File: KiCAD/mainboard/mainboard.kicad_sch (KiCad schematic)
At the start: 0 parts

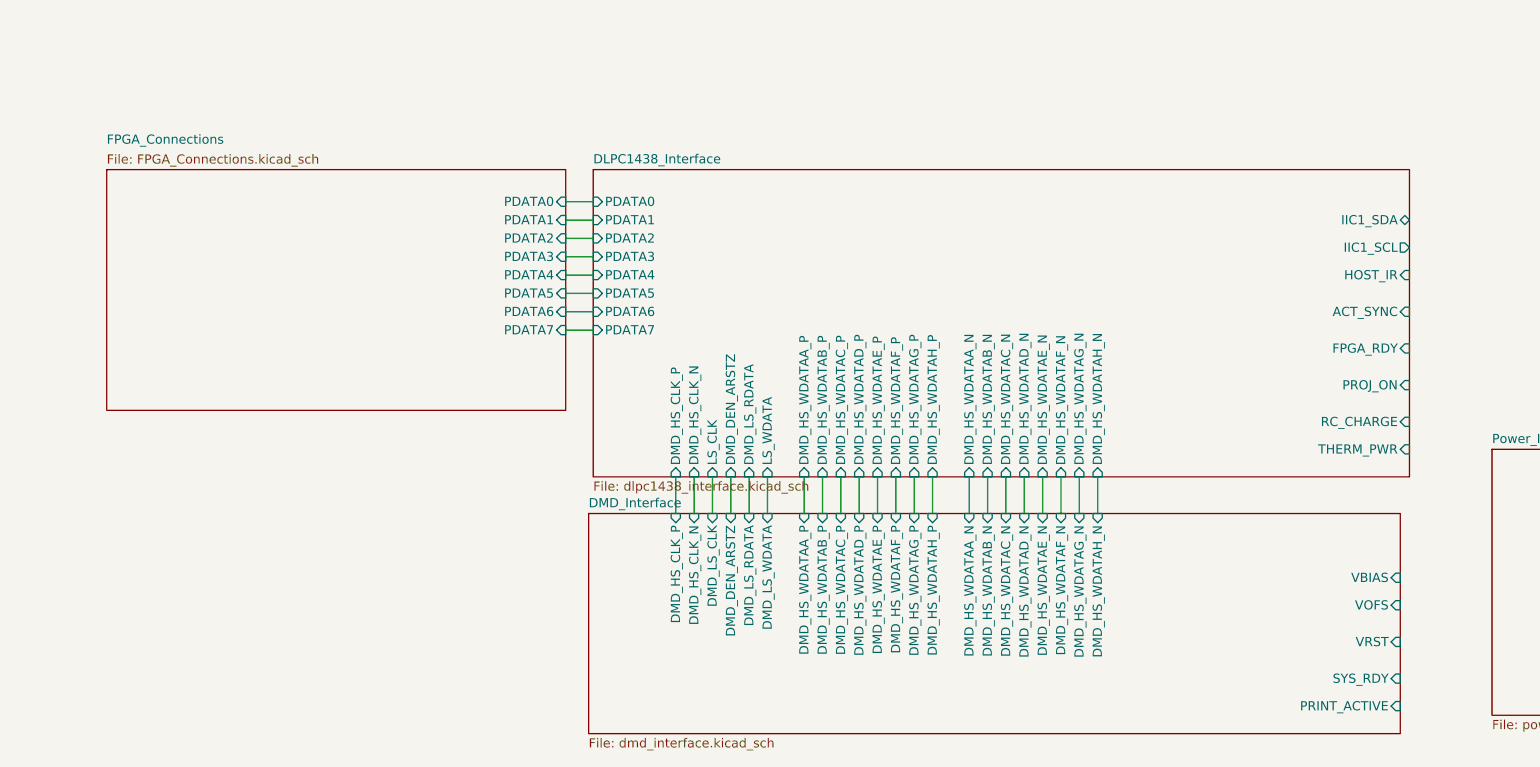
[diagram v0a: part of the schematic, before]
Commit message: fixed funny bus connectinos
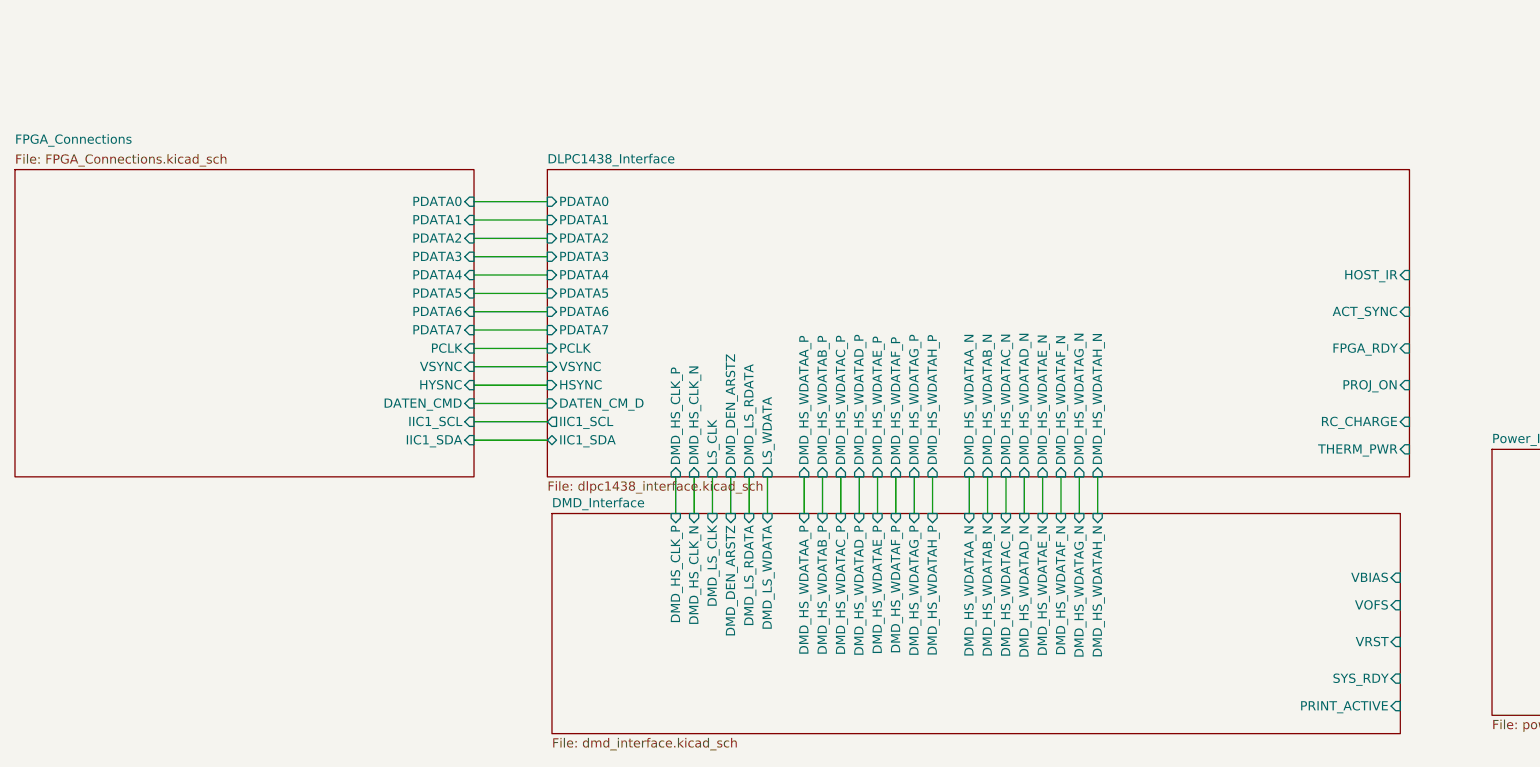
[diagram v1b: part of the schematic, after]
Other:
- sheet DLPC1438_Interface ports: added DATEN_CM_D, HSYNC, PCLK, VSYNC; removed none
- sheet FPGA_Connections ports: added DATEN_CMD, HYSNC, IIC1_SCL, IIC1_SDA, PCLK, VSYNC; removed none

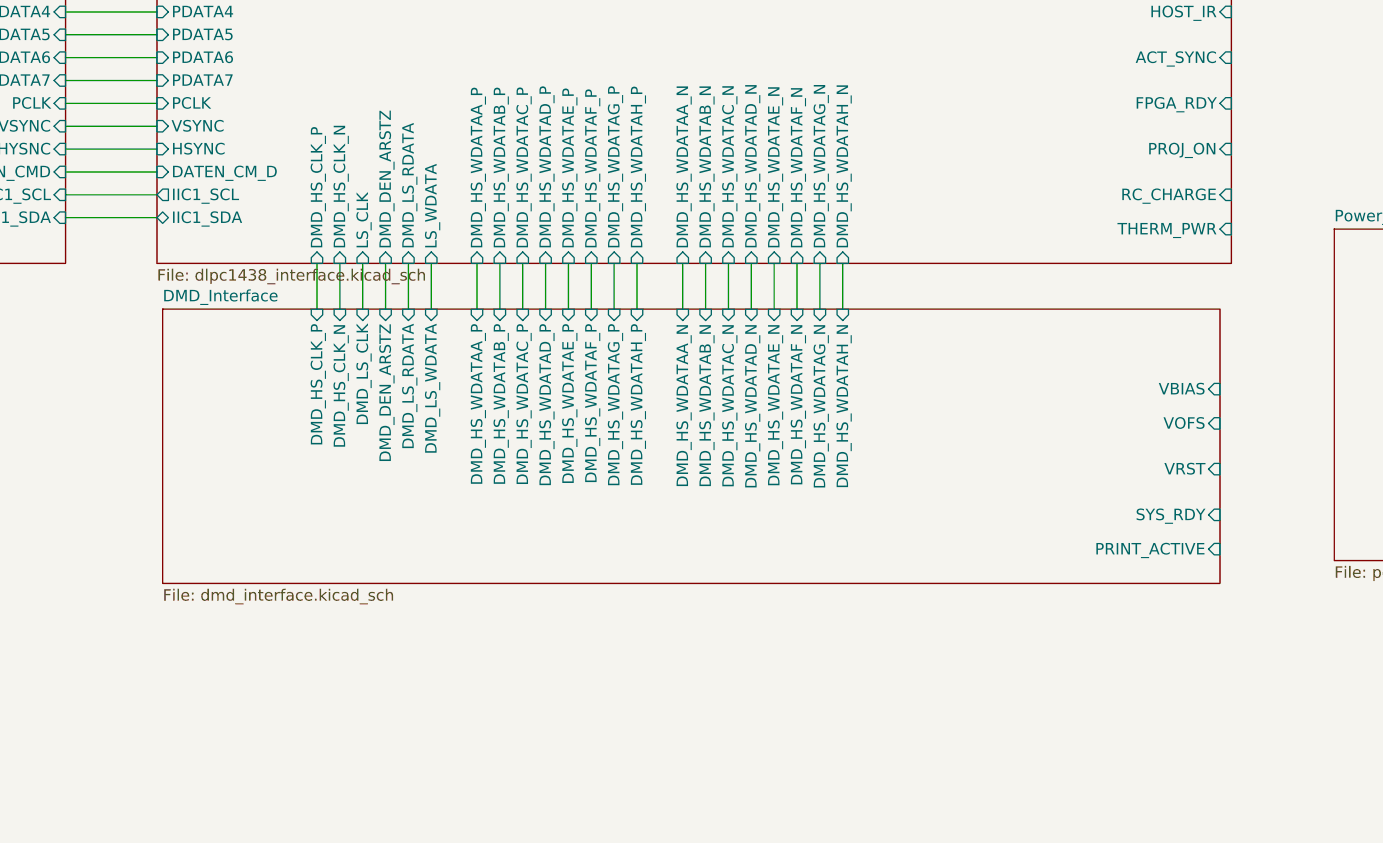
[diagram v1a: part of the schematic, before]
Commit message: gpios are now hierarchicals
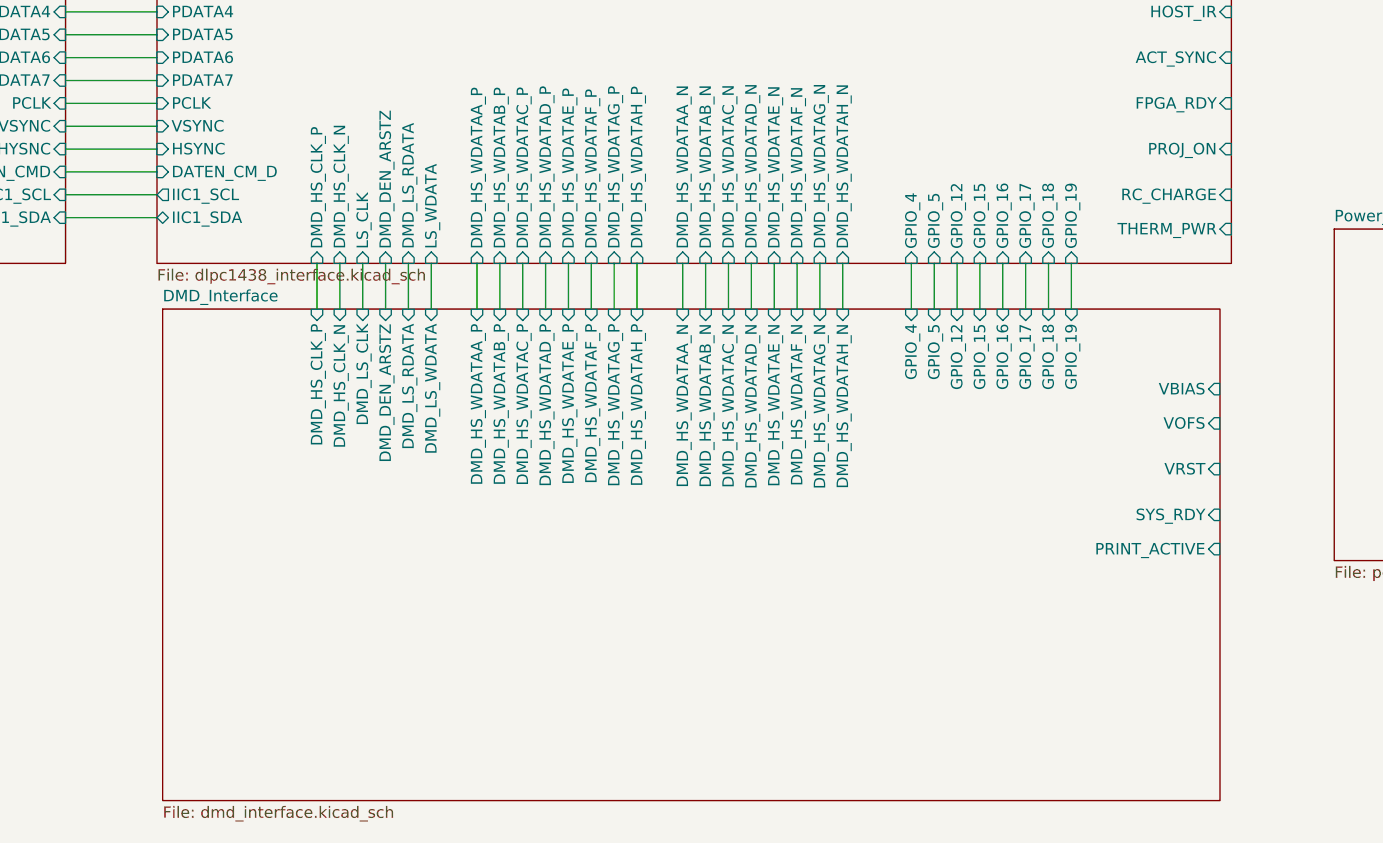
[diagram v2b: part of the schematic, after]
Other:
- sheet DLPC1438_Interface ports: added GPIO_12, GPIO_15, GPIO_16, GPIO_17, GPIO_18, GPIO_19, GPIO_4, GPIO_5; removed none
- sheet DMD_Interface ports: added GPIO_12, GPIO_15, GPIO_16, GPIO_17, GPIO_18, GPIO_19, GPIO_4, GPIO_5; removed none
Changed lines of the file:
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@@
+	(wire
+		(pts
+			(xy 265.43 281.94) (xy 265.43 287.02)
+		)
+		(stroke
+			(width 0)
+			(type default)
+		)
+	)
+	(wire
+		(pts
+			(xy 257.81 281.94) (xy 257.81 287.02)
+		)
+		(stroke
+			(width 0)
+			(type default)
+		)
+	)
 	(wire
 		(pts
@@
 	(wire
 		(pts
+			(xy 260.35 281.94) (xy 260.35 287.02)
+		)
+		(stroke
+			(width 0)
+			(type default)
+		)
+	)
+	(wire
+		(pts
 			(xy 161.29 251.46) (xy 171.45 251.46)
 		)
@@
 	(wire
 		(pts
+			(xy 255.27 281.94) (xy 255.27 287.02)
+		)
+		(stroke
+			(width 0)
+			(type default)
+		)
+	)
+	(wire
+		(pts
 			(xy 191.77 281.94) (xy 191.77 287.02)
 		)
@@
 	(wire
 		(pts
+			(xy 270.51 281.94) (xy 270.51 287.02)
+		)
+		(stroke
+			(width 0)
+			(type default)
+		)
+	)
+	(wire
+		(pts
 			(xy 161.29 256.54) (xy 171.45 256.54)
 		)
@@
 	(wire
 		(pts
+			(xy 267.97 281.94) (xy 267.97 287.02)
+		)
+		(stroke
+			(width 0)
+			(type default)
+		)
+	)
+	(wire
+		(pts
 			(xy 161.29 264.16) (xy 171.45 264.16)
 		)
@@
 	(wire
 		(pts
+			(xy 273.05 281.94) (xy 273.05 287.02)
+		)
+		(stroke
+			(width 0)
+			(type default)
+		)
+	)
+	(wire
+		(pts
 			(xy 207.01 281.94) (xy 207.01 287.02)
 		)
@@
 		(pts
 			(xy 224.79 281.94) (xy 224.79 287.02)
+		)
+		(stroke
+			(width 0)
+			(type default)
+		)
+	)
+	(wire
+		(pts
+			(xy 262.89 281.94) (xy 262.89 287.02)
 		)
 		(stroke
@@
 	(sheet
 		(at 172.085 287.02)
-		(size 117.475 30.48)
+		(size 117.475 54.61)
 		(exclude_from_sim no)
 		(in_bom yes)
@@
 		)
 		(property "Sheetfile" "dmd_interface.kicad_sch"
-			(at 172.085 318.0846 0)
+			(at 172.085 342.2146 0)
 			(effects
 				(font
@@
 		(pin "VRST" input
 			(at 289.56 304.8 0)
+			(effects
+				(font
+					(size 1.27 1.27)
+				)
+				(justify right)
+			)
+		)
+		(pin "GPIO_4" input
+			(at 255.27 287.02 90)
+			(effects
+				(font
+					(size 1.27 1.27)
+				)
+				(justify right)
+			)
+		)
+		(pin "GPIO_5" input
+			(at 257.81 287.02 90)
+			(effects
+				(font
+					(size 1.27 1.27)
+				)
+				(justify right)
+			)
+		)
+		(pin "GPIO_12" input
+			(at 260.35 287.02 90)
+			(effects
+				(font
+					(size 1.27 1.27)
+				)
+				(justify right)
+			)
+		)
+		(pin "GPIO_15" input
+			(at 262.89 287.02 90)
+			(effects
+				(font
+					(size 1.27 1.27)
+				)
+				(justify right)
+			)
+		)
+		(pin "GPIO_16" input
+			(at 265.43 287.02 90)
+			(effects
+				(font
+					(size 1.27 1.27)
+				)
+				(justify right)
+			)
+		)
+		(pin "GPIO_17" input
+			(at 267.97 287.02 90)
+			(effects
+				(font
+					(size 1.27 1.27)
+				)
+				(justify right)
+			)
+		)
+		(pin "GPIO_18" input
+			(at 270.51 287.02 90)
+			(effects
+				(font
+					(size 1.27 1.27)
+				)
+				(justify right)
+			)
+		)
+		(pin "GPIO_19" input
+			(at 273.05 287.02 90)
 			(effects
 				(font
@@
 			(effects
 				(font
+					(size 1.27 1.27)
+				)
+				(justify left)
+			)
+		)
+		(pin "GPIO_4" input
+			(at 255.27 281.94 270)
+			(effects
+				(font
+					(size 1.27 1.27)
+				)
+				(justify left)
+			)
+		)
+		(pin "GPIO_5" input
+			(at 257.81 281.94 270)
+			(effects
+				(font
+					(size 1.27 1.27)
+				)
+				(justify left)
+			)
+		)
+		(pin "GPIO_12" input
+			(at 260.35 281.94 270)
+			(effects
+				(font
+					(size 1.27 1.27)
+				)
+				(justify left)
+			)
+		)
+		(pin "GPIO_15" input
+			(at 262.89 281.94 270)
+			(effects
+				(font
+					(size 1.27 1.27)
+				)
+				(justify left)
+			)
+		)
+		(pin "GPIO_16" input
+			(at 265.43 281.94 270)
+			(effects
+				(font
+					(size 1.27 1.27)
+				)
+				(justify left)
+			)
+		)
+		(pin "GPIO_17" input
+			(at 267.97 281.94 270)
+			(effects
+				(font
+					(size 1.27 1.27)
+				)
+				(justify left)
+			)
+		)
+		(pin "GPIO_18" input
+			(at 270.51 281.94 270)
+			(effects
+				(font
+					(size 1.27 1.27)
+				)
+				(justify left)
+			)
+		)
+		(pin "GPIO_19" input
+			(at 273.05 281.94 270)
+			(effects
+				(font

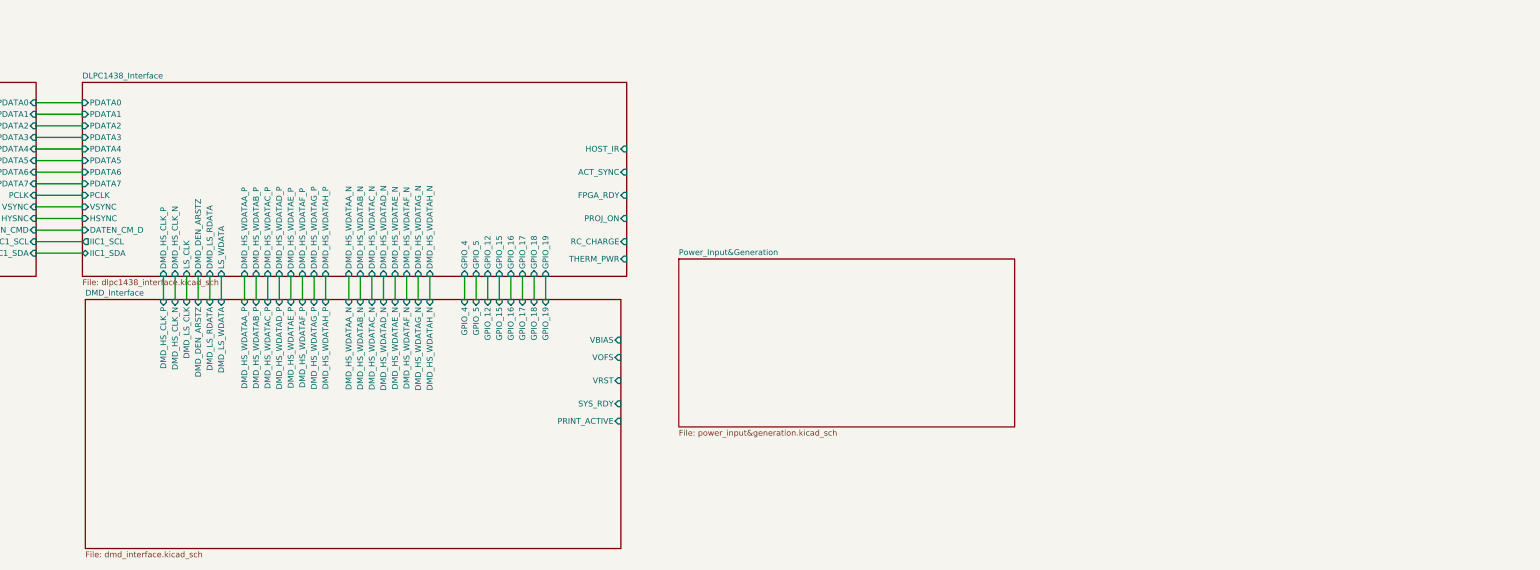
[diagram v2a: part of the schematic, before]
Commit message: fixed spi1 dlpc connections
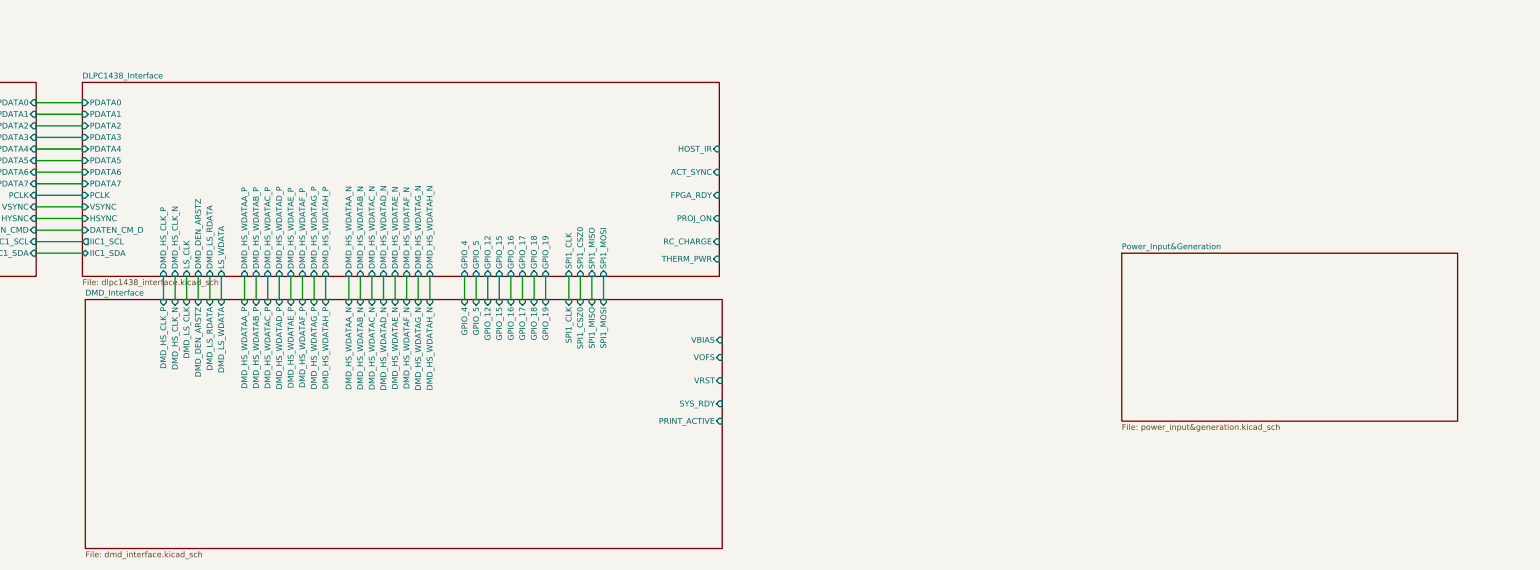
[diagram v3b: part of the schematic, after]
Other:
- sheet DLPC1438_Interface ports: added SPI1_CLK, SPI1_CSZ0, SPI1_MISO, SPI1_MOSI; removed none
- sheet DMD_Interface ports: added SPI1_CLK, SPI1_CSZ0, SPI1_MISO, SPI1_MOSI; removed none
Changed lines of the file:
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@@
+	(wire
+		(pts
+			(xy 285.75 281.94) (xy 285.75 287.02)
+		)
+		(stroke
+			(width 0)
+			(type default)
+		)
+	)
 	(wire
 		(pts
@@
 	(wire
 		(pts
+			(xy 280.67 281.94) (xy 280.67 287.02)
+		)
+		(stroke
+			(width 0)
+			(type default)
+		)
+	)
+	(wire
+		(pts
 			(xy 161.29 266.7) (xy 171.45 266.7)
 		)
@@
 	(wire
 		(pts
+			(xy 283.21 281.94) (xy 283.21 287.02)
+		)
+		(stroke
+			(width 0)
+			(type default)
+		)
+	)
+	(wire
+		(pts
 			(xy 199.39 281.94) (xy 199.39 287.02)
 		)
@@
 	(wire
 		(pts
+			(xy 278.13 281.94) (xy 278.13 287.02)
+		)
+		(stroke
+			(width 0)
+			(type default)
+		)
+	)
+	(wire
+		(pts
 			(xy 161.29 248.92) (xy 171.45 248.92)
 		)
@@
 	)
 	(sheet
-		(at 302.26 278.13)
+		(at 399.415 276.86)
 		(size 73.66 36.83)
 		(exclude_from_sim no)
@@
 		)
 		(property "Sheetname" "Power_Input&Generation"
-			(at 302.26 277.4184 0)
+			(at 399.415 276.1484 0)
 			(effects
 				(font
@@
 		)
 		(property "Sheetfile" "power_input&generation.kicad_sch"
-			(at 302.26 315.5446 0)
+			(at 399.415 314.2746 0)
 			(effects
 				(font
@@
 	(sheet
 		(at 172.085 287.02)
-		(size 117.475 54.61)
+		(size 139.7 54.61)
 		(exclude_from_sim no)
 		(in_bom yes)
@@
 		)
 		(pin "PRINT_ACTIVE" input
-			(at 289.56 313.69 0)
+			(at 311.785 313.69 0)
 			(effects
 				(font
@@
 		)
 		(pin "SYS_RDY" input
-			(at 289.56 309.88 0)
+			(at 311.785 309.88 0)
 			(effects
 				(font
@@
 		)
 		(pin "VBIAS" input
-			(at 289.56 295.91 0)
+			(at 311.785 295.91 0)
 			(effects
 				(font
@@
 		)
 		(pin "VOFS" input
-			(at 289.56 299.72 0)
+			(at 311.785 299.72 0)
 			(effects
 				(font
@@
 		)
 		(pin "VRST" input
-			(at 289.56 304.8 0)
+			(at 311.785 304.8 0)
 			(effects
 				(font
@@
 		(pin "GPIO_19" input
 			(at 273.05 287.02 90)
+			(effects
+				(font
+					(size 1.27 1.27)
+				)
+				(justify right)
+			)
+		)
+		(pin "SPI1_CLK" input
+			(at 278.13 287.02 90)
+			(effects
+				(font
+					(size 1.27 1.27)
+				)
+				(justify right)
+			)
+		)
+		(pin "SPI1_CSZ0" input
+			(at 280.67 287.02 90)
+			(effects
+				(font
+					(size 1.27 1.27)
+				)
+				(justify right)
+			)
+		)
+		(pin "SPI1_MISO" input
+			(at 283.21 287.02 90)
+			(effects
+				(font
+					(size 1.27 1.27)
+				)
+				(justify right)
+			)
+		)
+		(pin "SPI1_MOSI" input
+			(at 285.75 287.02 90)
 			(effects
 				(font
@@
 	(sheet
 		(at 171.45 239.395)
-		(size 119.38 42.545)
+		(size 139.7 42.545)
 		(exclude_from_sim no)
 		(in_bom yes)
@@
 		)
 		(pin "FPGA_RDY" input
-			(at 290.83 264.16 0)
+			(at 311.15 264.16 0)
 			(effects
 				(font
@@
 		)
 		(pin "PROJ_ON" input
-			(at 290.83 269.24 0)
+			(at 311.15 269.24 0)
 			(effects
 				(font
@@
 		)
 		(pin "RC_CHARGE" input
-			(at 290.83 274.32 0)
+			(at 311.15 274.32 0)
 			(effects
 				(font
@@
 		)
 		(pin "THERM_PWR" input
-			(at 290.83 278.13 0)
+			(at 311.15 278.13 0)
 			(effects
 				(font
@@
 		)
 		(pin "ACT_SYNC" input
-			(at 290.83 259.08 0)
+			(at 311.15 259.08 0)
 			(effects
 				(font
@@
 		)
 		(pin "HOST_IR" input
-			(at 290.83 254 0)
+			(at 311.15 254 0)
 			(effects
 				(font
@@
 			(effects
 				(font
+					(size 1.27 1.27)
+				)
+				(justify left)
+			)
+		)
+		(pin "SPI1_CLK" input
+			(at 278.13 281.94 270)
+			(effects
+				(font
+					(size 1.27 1.27)
+				)
+				(justify left)
+			)
+		)
+		(pin "SPI1_CSZ0" input
+			(at 280.67 281.94 270)
+			(effects
+				(font
+					(size 1.27 1.27)
+				)
+				(justify left)
+			)
+		)
+		(pin "SPI1_MISO" input
+			(at 283.21 281.94 270)
+			(effects
+				(font
+					(size 1.27 1.27)
+				)
+				(justify left)
+			)
+		)
+		(pin "SPI1_MOSI" input
+			(at 285.75 281.94 270)
+			(effects
+				(font
